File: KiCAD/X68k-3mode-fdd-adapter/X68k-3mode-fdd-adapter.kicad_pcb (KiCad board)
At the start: 4 copper layers, 129 x 100 mm, 134 parts, among them J1001 Barrel_Jack_Switch, J1003 USB_C_Receptacle_USB2.0_16P, J101 4pin, J102 Conn_02x06_Odd_Even, J103 Conn_01x02, J104 Conn_01x04, J105 Conn_01x02, J106 Conn_02x17_Odd_Even, J107 Conn_02x17_Odd_Even, J108 Conn_02x17_Odd_Even, Q1001 FDS4935A, Q1002 FDS4935A, Q1003 FDS4935A, Q101 DTC143Z, Q102 2SC2712, Q201 BSS138, Q301 BSS138, Q401 BSS138, Q501 BSS138, Q601 BSS138, Q701 BSS138, Q801 BSS138, Q901 BSS138, SW101 SW_DIP_x04, SW102 RESET_SW, U1001 K7805M-1000R3, U1002 MCP1792x-5002xCB, U101 INA3221AIRGVR, U102 SLG46826G(V2), U103 SLG46826G(V2), U104 CH32X035C8T6, U105 SLG46826G(V2)

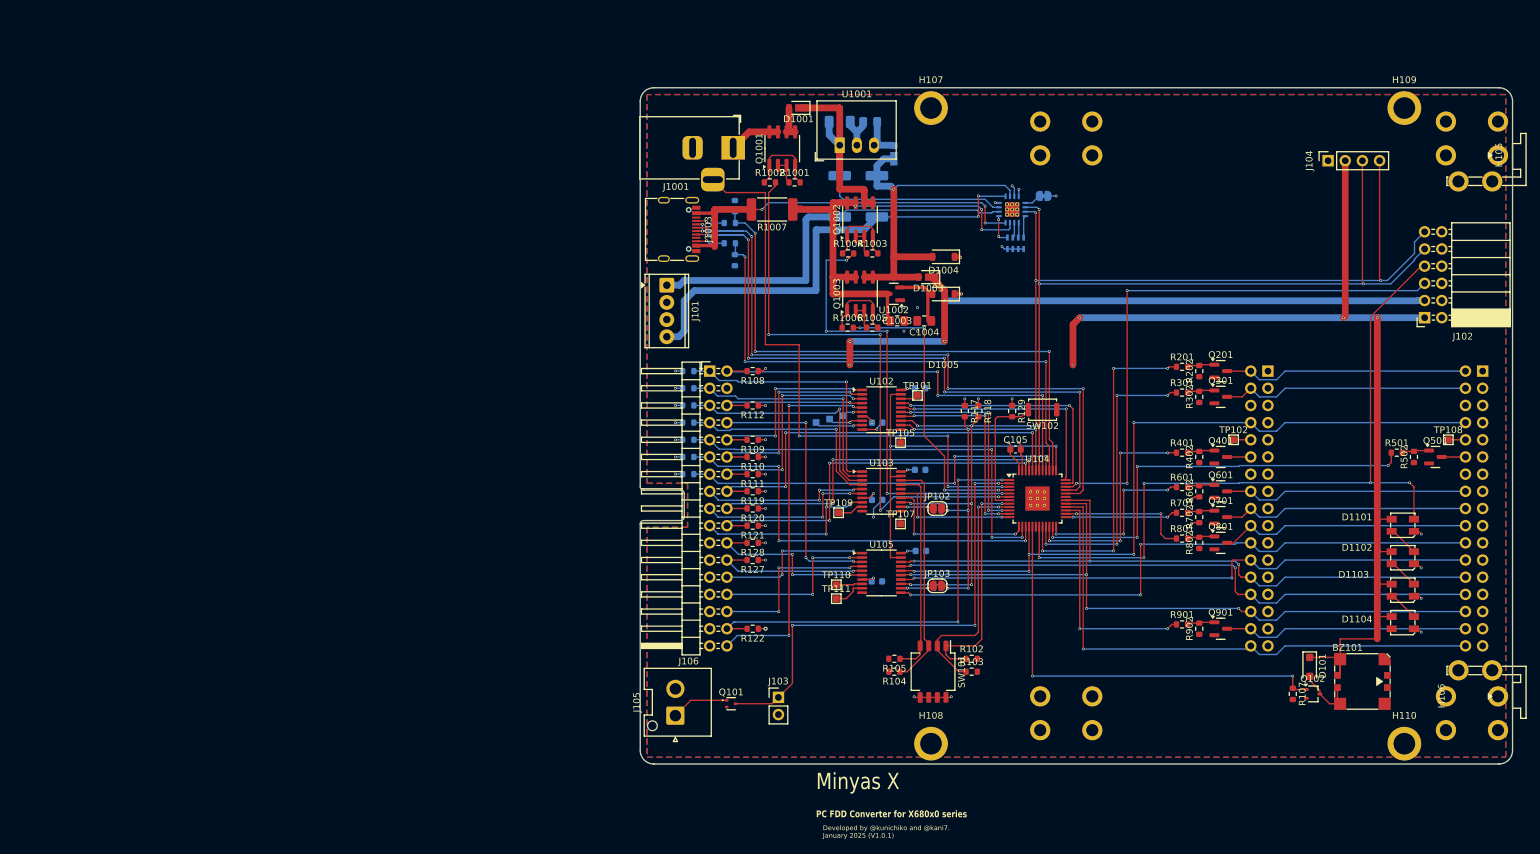
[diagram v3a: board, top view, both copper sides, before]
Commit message: 部品の配置、シルクを調整
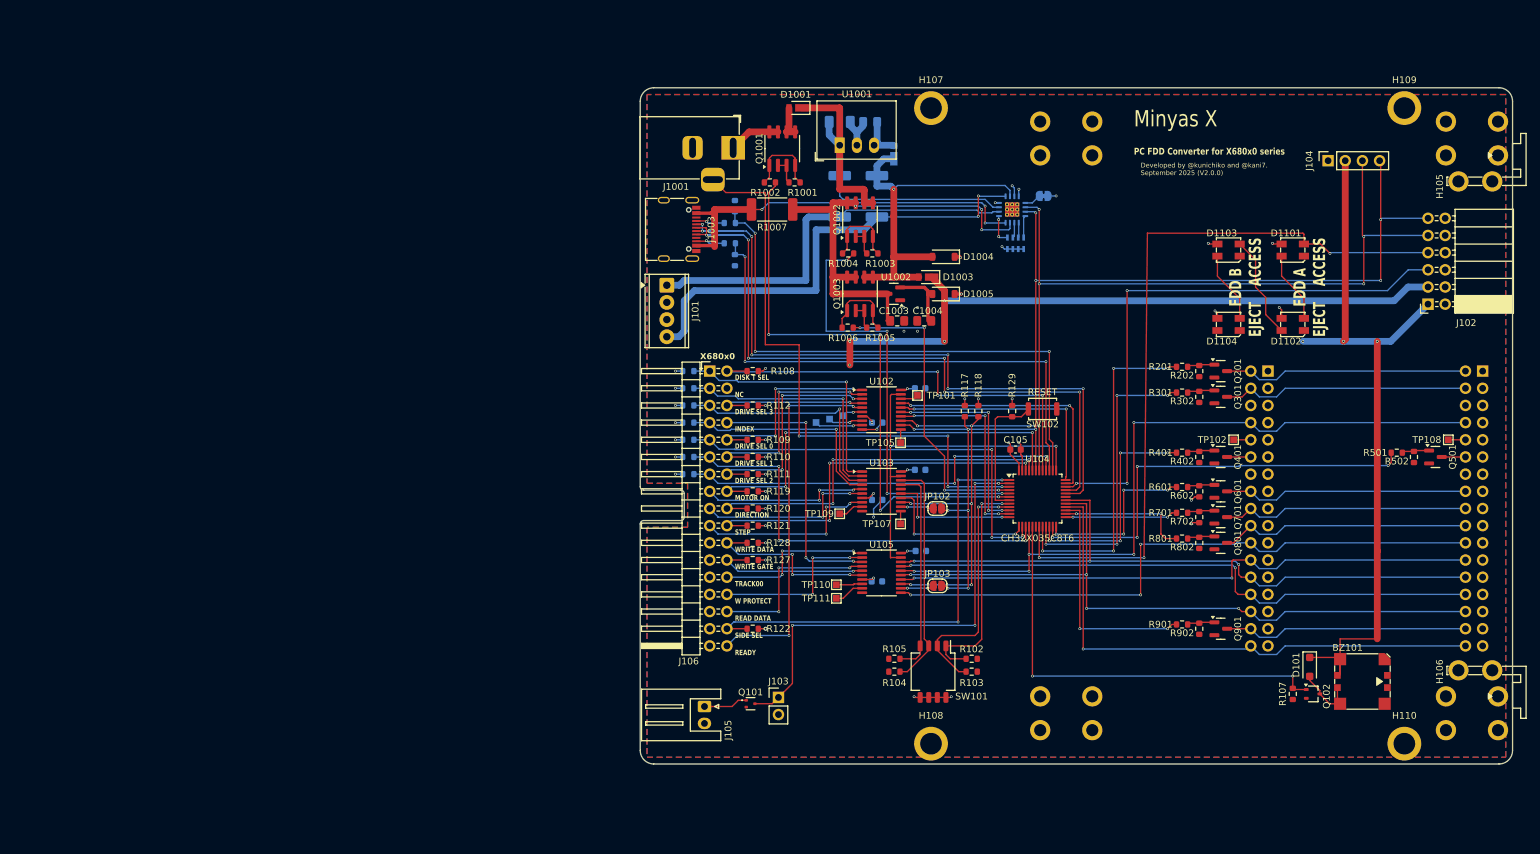
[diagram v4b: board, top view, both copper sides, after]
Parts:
- J105: footprint Connector_JST:JST_VH_B2P-VH-FB-B_1x02_P3.96mm_Vertical -> Connector_JST:JST_XH_S2B-XH-A_1x02_P2.50mm_Horizontal
- SW102: value RESET_SW -> RESET
- U104: footprint Package_QFP:LQFP-48-1EP_7x7mm_P0.5mm_EP3.6x3.6mm_ThermalVias -> Package_QFP:LQFP-48_7x7mm_P0.5mm
- moved D1103 56.5 mm to (158.0, 71.0)
- moved D1104 51.1 mm to (158.0, 82.0)
- moved D1101 43.8 mm to (167.5, 71.0)
- moved D1102 38.1 mm to (167.5, 82.0)
- moved J105 4.51 mm to (80.5, 138.5), turned to -90 degrees
- moved Q101 2.87 mm to (87.3, 138.1)
- moved J102 2.06 mm to (187.5, 79.0)
- moved TP109 0.22 mm to (100.5, 110.0)
- moved SW102 0.11 mm to (130.5, 94.5)
- moved TP111 0.06 mm to (100.0, 122.5)
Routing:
- net VDD_MCU: track 182.3 -> 142.1 mm, vias 18 -> 21
- net Net-(D1102-DOUT): track 4.54 -> 15.4 mm
- net Net-(D1103-DOUT): track 4.54 -> 10.6 mm
- net Net-(D1101-DOUT): track 4.54 -> 10.6 mm
- net GND: track 26.4 -> 21.1 mm, vias 15 -> 11
- net /I2C_SDA: track 172.8 -> 169.5 mm, vias 10 -> 11
- net /X68k_PWR: track 71.3 -> 68.5 mm
- net Net-(J105-Pin_1): track 8.54 -> 6.55 mm
- net VDD_FDDIF: track 125.7 -> 127.6 mm
- net /CONTROLLER_OPTION: track 82.2 -> 83.6 mm
- net /I2C_SCL: track 185.4 -> 184.2 mm, vias 10 -> 11
- net /VBUS: track 67.0 -> 66.1 mm
- net /LED_DATA: track 111.7 -> 112.1 mm, vias 5 -> 3
- net /+12V_ENABLE_n: vias 5 -> 4
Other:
- board text added: "D IN ERR D F INT GND GND GND GND GND GND GND"
- board text added: "Developed by @kunichiko and @kani7. September 2025 (V2.0.0)"
- board text added: "FDD A EJECT ACCESS"
- board text added: "FDD B EJECT ACCESS"
- board text added: "MODE SEL IN USE NC INDEX DRIVE SEL 0 DRIVE SEL 1 NC MOTOR ON DIRECTION STEP WRITE DATA WRITE GATE TRACK00 W PROTECT READ DATA SIDE SEL DISK CHG"
- board text added: "OPT 0 OPT 1 OPT 2 OPT 3 EJECT E MASK L BLINK"
- board text removed: "Developed by @kunichiko and @kani7. January 2025 (V1.0.1)"
- board text removed: "MODE SEL NC NC INDEX DRIVE SEL 0 DRIVE SEL 1 NC MOTOR ON DIRECTION STEP WRITE DATA WRITE GATE TRACK00 W PROTECT READ DATA SIDE SEL DISK CHG"
- board text removed: "OPT 0 OPT 1 OPT 2 OPT 3 EJECT EJECT MASK LED BLINK DISK IN ERR DISK FDD INT GND GND GND GND GND GND GND"

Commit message: シルクをさらに調整
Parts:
- renumbered H107 to H105, H108 to H106, H109 to H107, H110 to H108, H105 to H109, H106 to H110, J1003 to J1002, J107 to J106, J106 to J107, R1010 to R1009, R1012 to R1010, R1013 to R1011, R124 to R123, R125 to R124, R126 to R125, R127 to R126, R128 to R127, R129 to R128
